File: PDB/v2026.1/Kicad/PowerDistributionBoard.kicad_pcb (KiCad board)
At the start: 2 copper layers, 184.8 x 112.4 mm, 77 parts, among them J1 Conn_02x01_12V_EXP3, J10 Conn_02x02_BMS, J11 Conn_02x02_IMD, J12 Conn_02x02_Suspension_Linear_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, J13 Conn_02x02_Suspension_Linear_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, J14 Conn_02x02_Suspension_Linear_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, J15 Conn_02x02_Suspension_Linear_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, J16 Conn_02x05_CCM_Faults, J17 EXP1_5V, J18 RasPI_5V, J19 LATCH_12V, J2 Conn_02x01_12V_EXP2, J20 Throttle_Sensor, J21 Conn_02x02_Current_Sensor, J22 Conn_02x02_Brake_Sensor1, J23 Conn_02x02_Brake_Sensor2, J24 Conn_02x02_Wheel_Sensor1, J25 Conn_02x02_Wheel_Sensor2, J26 Conn_02x01_3V_EXP, J27 BATTERY_12V, J28 BATTERY_GND, J29 BATTERY_24V, J3 Conn_02x01_12V_EXP, J31 FAN1_24V, J32 FAN2_24V, J33 PUMP1_24V, J34 PUMP2_24V, J35 24V_EXP1, J4 Conn_02x01_RTM, J5 CCM_12V, J7 Conn_02x02_BSPD, J8 Conn_02x02_LATCH, J9 Conn_02x02_TSSI, U1 5to3.3_Linear_Regulator, U2 TLV76150DCYR

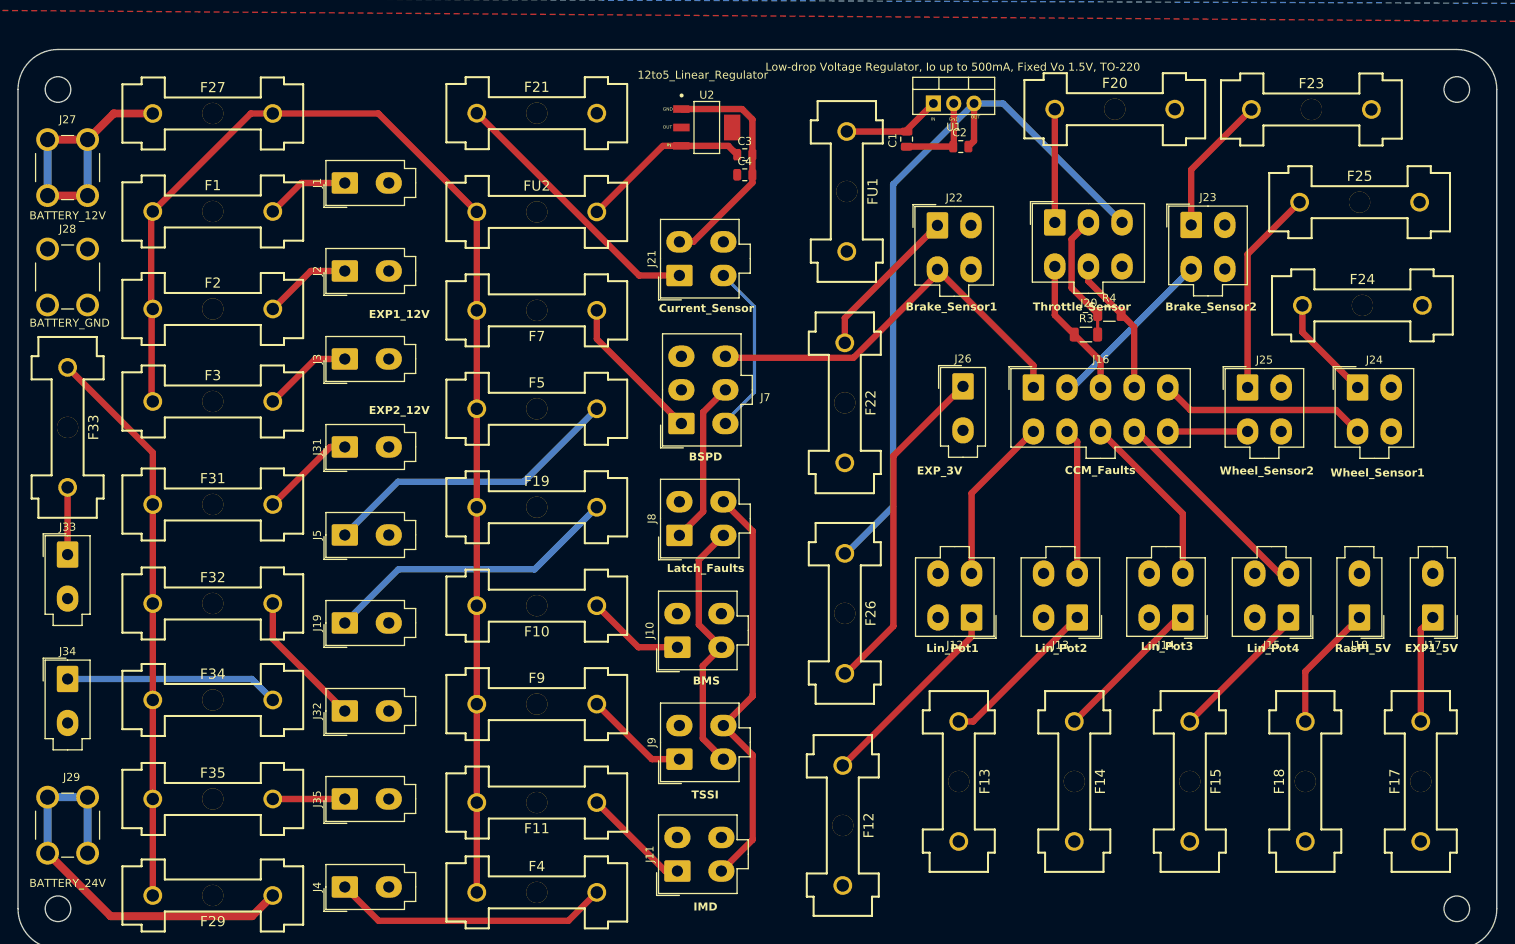
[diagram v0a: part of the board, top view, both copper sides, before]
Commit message: Silkscreen pin assignment now easier
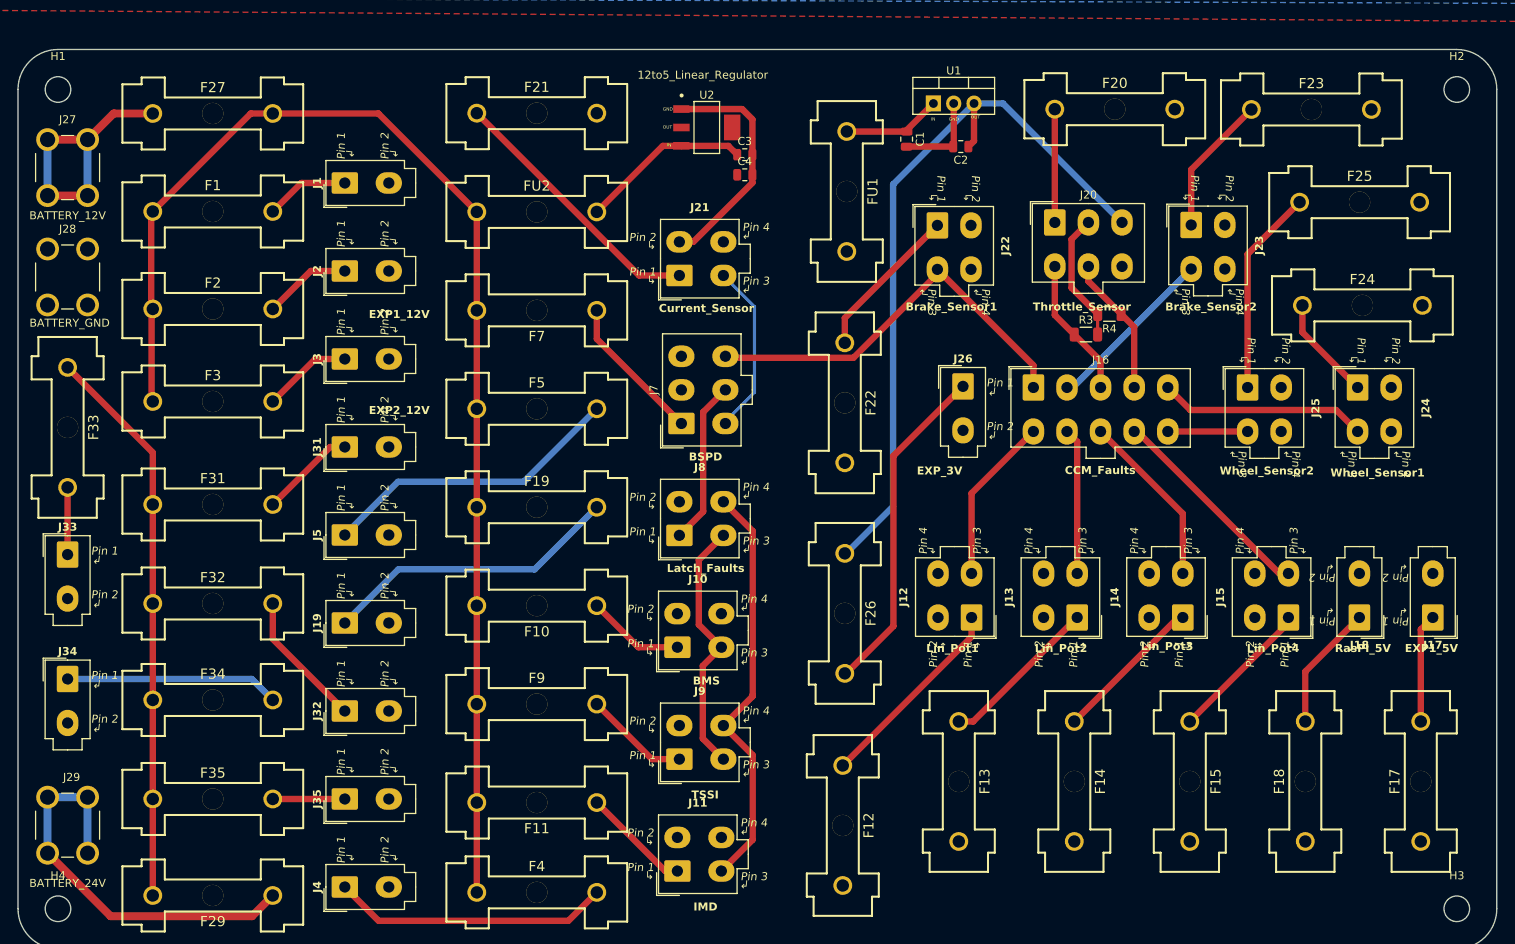
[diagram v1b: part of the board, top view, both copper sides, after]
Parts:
- H1, H2, H3, H4: value MountingHole -> MountingHole M3
- J1: value Conn_02x01_12V_EXP3 -> 12V_EXP3
- J12: value Conn_02x02_Suspension_Linear_Pot1 -> Suspension_Linear_Pot1
- J13: value Conn_02x02_Suspension_Linear_Pot2 -> Suspension_Linear_Pot2
- J14: value Conn_02x02_Suspension_Linear_Pot3 -> Suspension_Linear_Pot3
- J15: value Conn_02x02_Suspension_Linear_Pot4 -> Suspension_Linear_Pot4
- J2: value Conn_02x01_12V_EXP2 -> 12V_EXP2
- J22: value Conn_02x02_Brake_Sensor1 -> Brake_Sensor1
- J23: value Conn_02x02_Brake_Sensor2 -> Brake_Sensor2
- J24: value Conn_02x02_Wheel_Sensor1 -> Wheel_Sensor1
- J25: value Conn_02x02_Wheel_Sensor2 -> Wheel_Sensor2
- J26: value Conn_02x01_3V_EXP -> 3V3_EXP
- J3: value Conn_02x01_12V_EXP -> 12V_EXP1
- J4: value Conn_02x01_RTM -> RTM
- J7: value Conn_02x02_BSPD -> BSPD
- J8: value Conn_02x02_LATCH -> LATCH
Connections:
- net Net-(J1-Pin_1) renamed /Fuse_EXP3_12V
- net Net-(J12-Pin_1) renamed /Fuse_Lin_Pot1
- net Net-(J2-Pin_1) renamed /Fuse_EXP2_12V
- net Net-(J20-Pin_1) renamed /Fuse_Throttle
- net Net-(J26-Pin_1) renamed /Fuse_EXP_3V3
- net Net-(J27-Pin_1) renamed /Fuse_Batt12V
- net Net-(J29-Pin_1) renamed /Fuse_Batt24V
- net Net-(J3-Pin_1) renamed /Fuse_EXP1_12V
- net Net-(J4-Pin_1) renamed /Fuse_RTM
- net Net-(J7-Pin_1) renamed /Fuse_BSPD

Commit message: Restored step files
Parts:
- J16: footprint Connector_Molex:Molex_Mini-Fit_Jr_5566-10A_2x05_P4.20mm_Vertical -> 0footprints:Molex_Mini-Fit_Jr_5566-10A_2x05_P4.20mm_Vertical
- J20, J7: footprint Connector_Molex:Molex_Mini-Fit_Jr_5566-06A_2x03_P4.20mm_Vertical -> 0footprints:Molex_Mini-Fit_Jr_5566-06A_2x03_P4.20mm_Vertical
- J27, J28, J29: footprint TerminalBlock:KEYSTONE_7797 -> 0footprints:KEYSTONE_7797
- U2: footprint Converter_DCDC:DCY0004A-IPC_A -> Package_TO_SOT_SMD:SOT-223
- moved C4 1.30 mm to (141.0, 41.3)
- moved C3 1.27 mm to (141.0, 38.7)
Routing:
- net GND: track 57.4 -> 58.3 mm
- net Net-(U2-IN): track 21.4 -> 22.0 mm

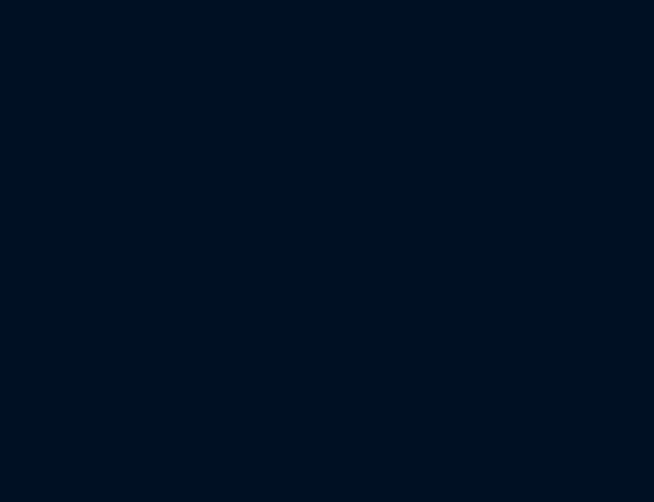
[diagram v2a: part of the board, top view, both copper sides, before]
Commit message: Updated throttle sensors, marked 24V components DNP
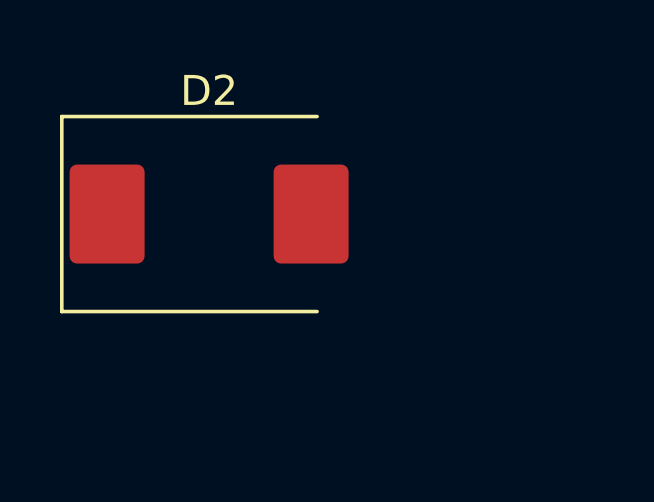
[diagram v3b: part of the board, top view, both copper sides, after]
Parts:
- added D2: 1.5SMCxxA, Diode_SMD:D_SMC, F.Cu at (-55.0, -9.53)
- J10: value Conn_02x02_BMS -> BMS
- J11: value Conn_02x02_IMD -> IMD
- J16: value Conn_02x05_CCM_Faults -> CCM_Faults
- J21: value Conn_02x02_Current_Sensor -> Current_Sensor
- J9: value Conn_02x02_TSSI -> TSSI
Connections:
- J16 pad 3: Throttle_Sensor_Vout -> Throttle_Sensor_Vout1
- J20 pad 6: unconnected-(J20-Pin_6-Pad6) -> GND

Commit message: Added labels for every net
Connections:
- net Net-(J10-Pin_1) renamed /Fuse_BMMS
- net Net-(J11-Pin_1) renamed /Fuse_IMD
- net Net-(J13-Pin_1) renamed /Fuse_Lin_Pot2
- net Net-(J14-Pin_1) renamed /Fuse_Lin_Pot3
- net Net-(J15-Pin_1) renamed /Fuse_Lin_Pot4
- net Net-(J21-Pin_1) renamed /Fuse_CurrentSensor
- net Net-(J22-Pin_1) renamed /Fuse_Break1
- net Net-(J23-Pin_1) renamed /Fuse_Break2
- net Net-(J24-Pin_1) renamed /Fuse_Wheel1
- net Net-(J25-Pin_1) renamed /Fuse_Wheel2
- net Net-(J31-Pin_1) renamed /Fuse_Fan1
- net Net-(J32-Pin_1) renamed /Fuse_Fan2
- net Net-(J33-Pin_1) renamed /Fuse_Pump1
- net Net-(J34-Pin_1) renamed /Fuse_Pump2
- net Net-(J35-Pin_1) renamed /Fuse_EXP1_24V
- net Net-(J9-Pin_1) renamed /Fuse_TSSI
- net Net-(U1-VI) renamed /Fuse_5to3.3
- net Net-(U2-IN) renamed /Fuse_12to5

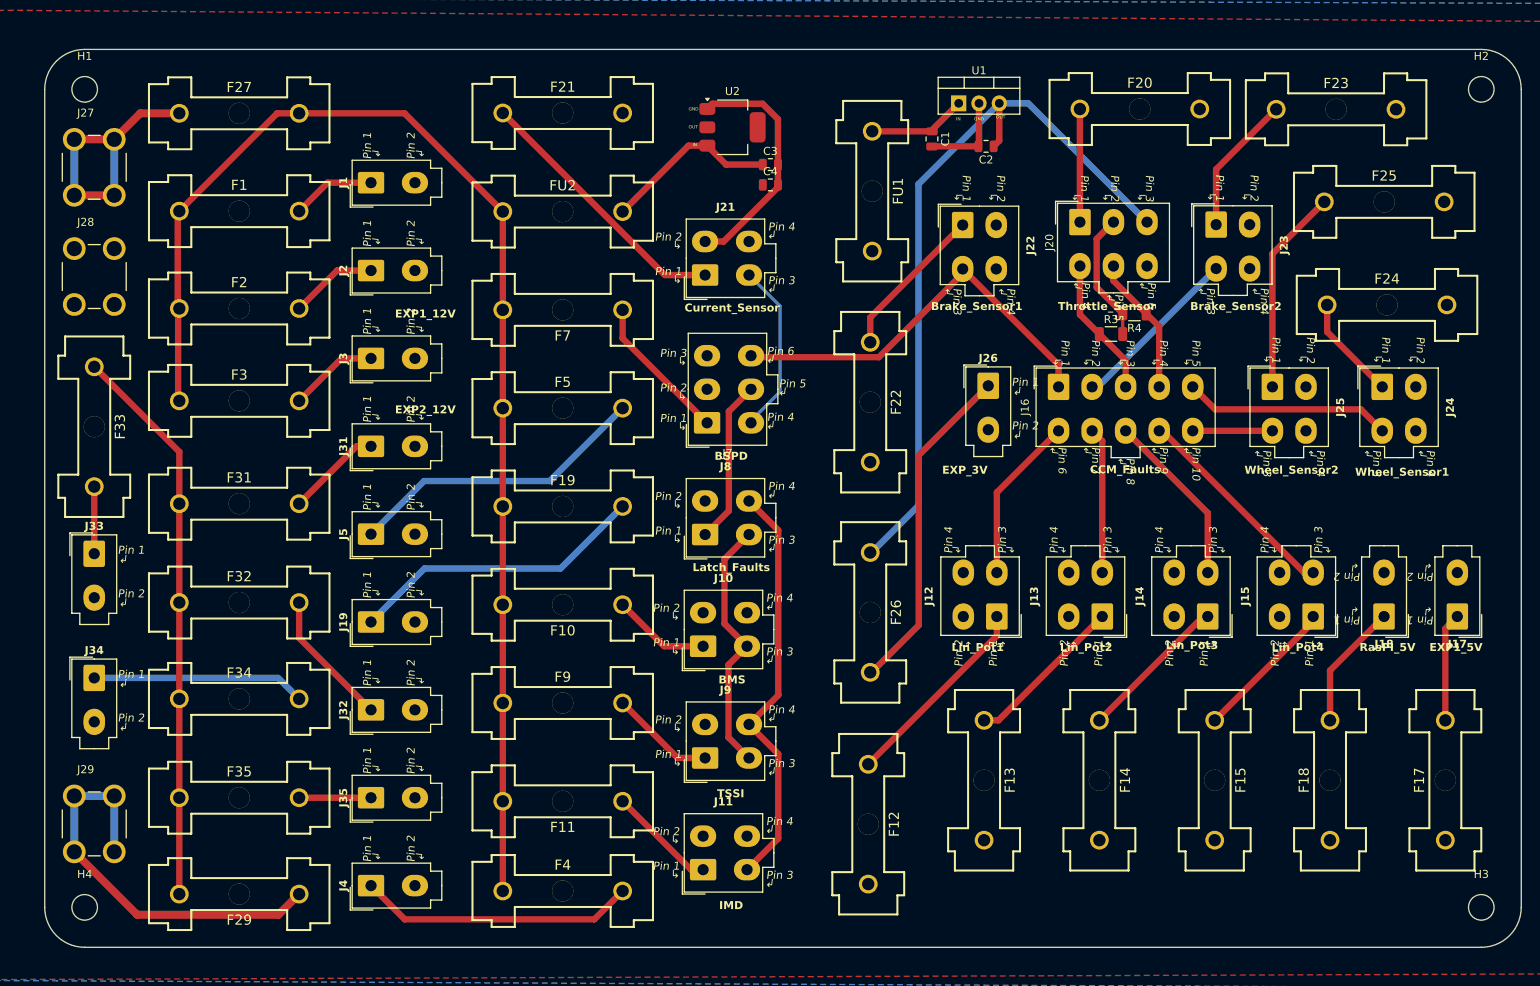
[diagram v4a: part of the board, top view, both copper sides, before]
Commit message: Started labeling each pin
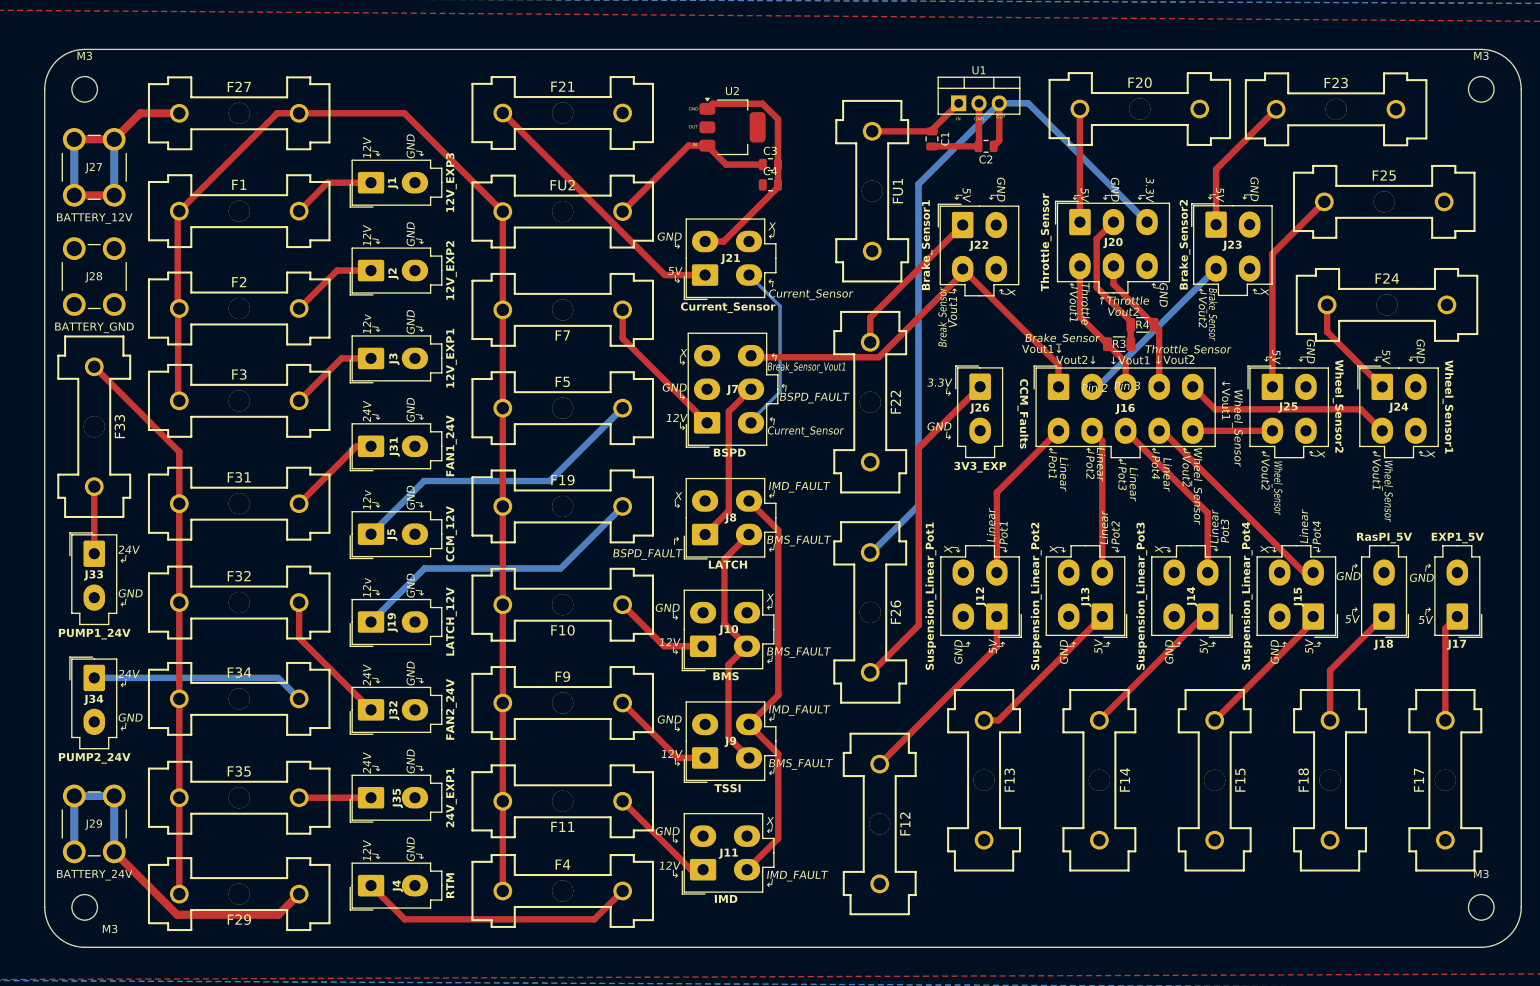
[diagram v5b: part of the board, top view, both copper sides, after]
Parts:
- moved R4 1.74 mm to (187.6, 58.8)
- moved R3 1.63 mm to (184.7, 61.2)
- moved F12 1.44 mm to (154.7, 121.3)
- moved J26 1.02 mm to (167.3, 66.5)
- renumbered H3 to M3, H1 to M3, H4 to M3, H2 to M3
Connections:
- J20 pad 4: Throttle_Sensor_Vout -> Throttle_Sensor_Vout1
- R3 pad 1: Throttle_Sensor_Vout -> Throttle_Sensor_Vout1
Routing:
- net Throttle_Sensor_Vout1: track 0.00 -> 17.5 mm
- net Throttle_Sensor_Vout: track 17.5 -> 0.00 mm
- net /Fuse_Batt24V: track 51.5 -> 46.5 mm
- net GND: track 58.3 -> 59.9 mm
- net /Fuse_Lin_Pot1: track 25.2 -> 24.5 mm
- net /Fuse_EXP_3V3: track 41.9 -> 41.4 mm
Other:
- board text removed: "BMS"
- board text removed: "BSPD"
- board text removed: "Brake_Sensor1"
- board text removed: "Brake_Sensor2"
- board text removed: "CCM_Faults"
- board text removed: "Current_Sensor"
- board text removed: "EXP1_12V"
- board text removed: "EXP1_5V"
- board text removed: "EXP2_12V"
- board text removed: "EXP_3V"
- board text removed: "IMD"
- board text removed: "Latch_Faults"
- board text removed: "Lin_Pot1"
- board text removed: "Lin_Pot2"
- board text removed: "Lin_Pot3"
- board text removed: "Lin_Pot4"
- board text removed: "RasPI_5V"
- board text removed: "TSSI"
- board text removed: "There are naming differences between J2 and J3, between their reference and the attatched silkscreen label name"
- board text removed: "Throttle_Sensor"
- board text removed: "Wheel_Sensor1"
- board text removed: "Wheel_Sensor2"
